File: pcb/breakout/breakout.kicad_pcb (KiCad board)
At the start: 2 copper layers, 19 x 19 mm, 6 parts, among them J1 ROW, J2 ROW, J3 COL, J4 COL, SW1 SW_DIP_x01

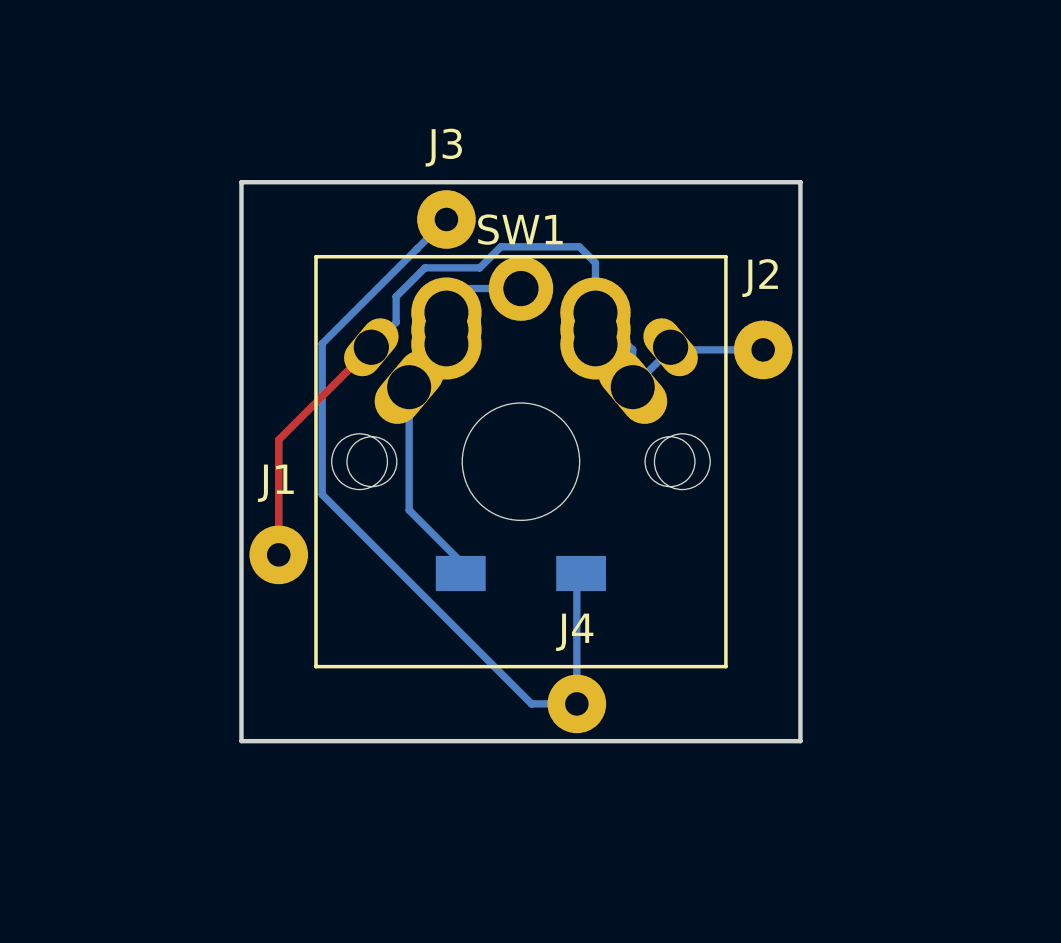
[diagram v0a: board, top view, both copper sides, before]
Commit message: breakout: improve silk
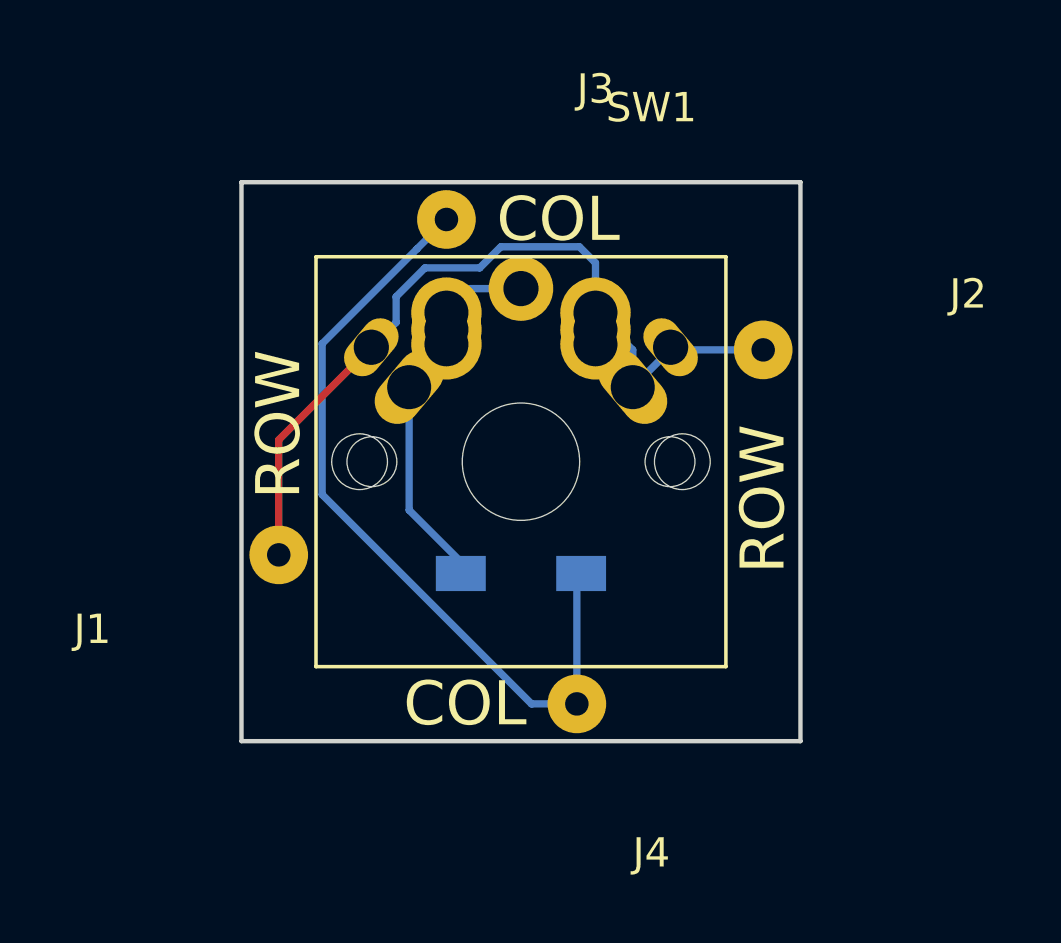
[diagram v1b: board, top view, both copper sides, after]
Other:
- board text added: "COL"
- board text added: "ROW"
- board text added: "SOD-23 Diode"
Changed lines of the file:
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@@
     (area 122.479999 96.444999 141.680001 115.645001)
     (thickness 1.6)
-    (drawings 4)
+    (drawings 13)
     (tracks 30)
     (zones 0)
@@
     (tags SOD-123)
     (attr smd)
-    (fp_text reference D1 (at 0 2) (layer B.SilkS)
+    (fp_text reference D1 (at 0 9.525) (layer B.SilkS)
       (effects (font (size 1 1) (thickness 0.15)) (justify mirror))
     )
@@
   (module Wire_Pads:SolderWirePad_single_0-8mmDrill (layer F.Cu)
     (at 123.825 109.22)
-    (fp_text reference J1 (at 0 -2.54) (layer F.SilkS)
+    (fp_text reference J1 (at -6.35 2.54) (layer F.SilkS)
       (effects (font (size 1 1) (thickness 0.15)))
     )
@@
   (module Wire_Pads:SolderWirePad_single_0-8mmDrill (layer F.Cu)
     (at 140.335 102.235)
-    (fp_text reference J2 (at 0 -2.54) (layer F.SilkS)
+    (fp_text reference J2 (at 6.985 -1.905) (layer F.SilkS)
       (effects (font (size 1 1) (thickness 0.15)))
     )
@@
   (module Wire_Pads:SolderWirePad_single_0-8mmDrill (layer F.Cu)
     (at 129.54 97.79)
-    (fp_text reference J3 (at 0 -2.54) (layer F.SilkS)
+    (fp_text reference J3 (at 5.08 -4.445) (layer F.SilkS)
       (effects (font (size 1 1) (thickness 0.15)))
     )
@@
   (module Wire_Pads:SolderWirePad_single_0-8mmDrill (layer F.Cu)
     (at 133.985 114.3)
-    (fp_text reference J4 (at 0 -2.54) (layer F.SilkS)
+    (fp_text reference J4 (at 2.54 5.08) (layer F.SilkS)
       (effects (font (size 1 1) (thickness 0.15)))
     )
@@
     (descr "Cherry MX keyswitch, MX1A, 1u, PCB mount, http://cherryamericas.com/wp-content/uploads/2014/12/mx_cat.pdf")
     (tags "cherry mx keyswitch MX1A 1u PCB")
-    (fp_text reference SW1 (at 0 -7.874) (layer F.SilkS)
+    (fp_text reference SW1 (at 4.445 -12.065) (layer F.SilkS)
       (effects (font (size 1 1) (thickness 0.15)))
     )
@@
       (effects (font (size 1 1) (thickness 0.15)))
     )
-    (fp_text user %R (at 0 -7.874) (layer F.Fab)
+    (fp_text user %R (at 8.255 -12.7) (layer F.Fab)
       (effects (font (size 1 1) (thickness 0.15)))
     )
@@
       (rotate (xyz 0 0 0))
     )
+  )
+  (gr_text "SOD-23 Diode" (at 132.08 111.76) (layer B.SilkS)
+    (effects (font (size 1 1) (thickness 0.2)) (justify mirror))
+  )
+  (gr_text COL (at 133.35 97.79) (layer B.SilkS)
+    (effects (font (size 1.5 1.5) (thickness 0.3)) (justify mirror))
+  )
+  (gr_text COL (at 130.175 114.3) (layer B.SilkS)
+    (effects (font (size 1.5 1.5) (thickness 0.3)) (justify mirror))
+  )
+  (gr_text ROW (at 123.825 104.775 90) (layer B.SilkS)
+    (effects (font (size 1.5 1.5) (thickness 0.3)) (justify mirror))
+  )
+  (gr_text ROW (at 140.335 107.315 90) (layer B.SilkS)
+    (effects (font (size 1.5 1.5) (thickness 0.3)) (justify mirror))
+  )
+  (gr_text ROW (at 123.825 104.775 90) (layer F.SilkS)
+    (effects (font (size 1.5 1.5) (thickness 0.3)))
+  )
+  (gr_text ROW (at 140.335 107.315 90) (layer F.SilkS)
+    (effects (font (size 1.5 1.5) (thickness 0.3)))
+  )
+  (gr_text "COL\n" (at 130.175 114.3) (layer F.SilkS)
+    (effects (font (size 1.5 1.5) (thickness 0.3)))
+  )
+  (gr_text COL (at 133.35 97.79) (layer F.SilkS)
+    (effects (font (size 1.5 1.5) (thickness 0.3)))
   )
   (gr_line (start 122.555 96.52) (end 141.605 96.52) (layer Edge.Cuts) (width 0.15))
@@
     (connect_pads (clearance 0.508))
     (min_thickness 0.254)
-    (fill yes (arc_segments 16) (thermal_gap 0.508) (thermal_bridge_width 0.508))
+    (fill (arc_segments 16) (thermal_gap 0.508) (thermal_bridge_width 0.508))
     (polygon
       (pts
@@
     (connect_pads (clearance 0.508))
     (min_thickness 0.254)
-    (fill yes (arc_segments 16) (thermal_gap 0.508) (thermal_bridge_width 0.508))
+    (fill (arc_segments 16) (thermal_gap 0.508) (thermal_bridge_width 0.508))
     (polygon
       (pts
